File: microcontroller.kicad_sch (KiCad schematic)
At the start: 0 parts

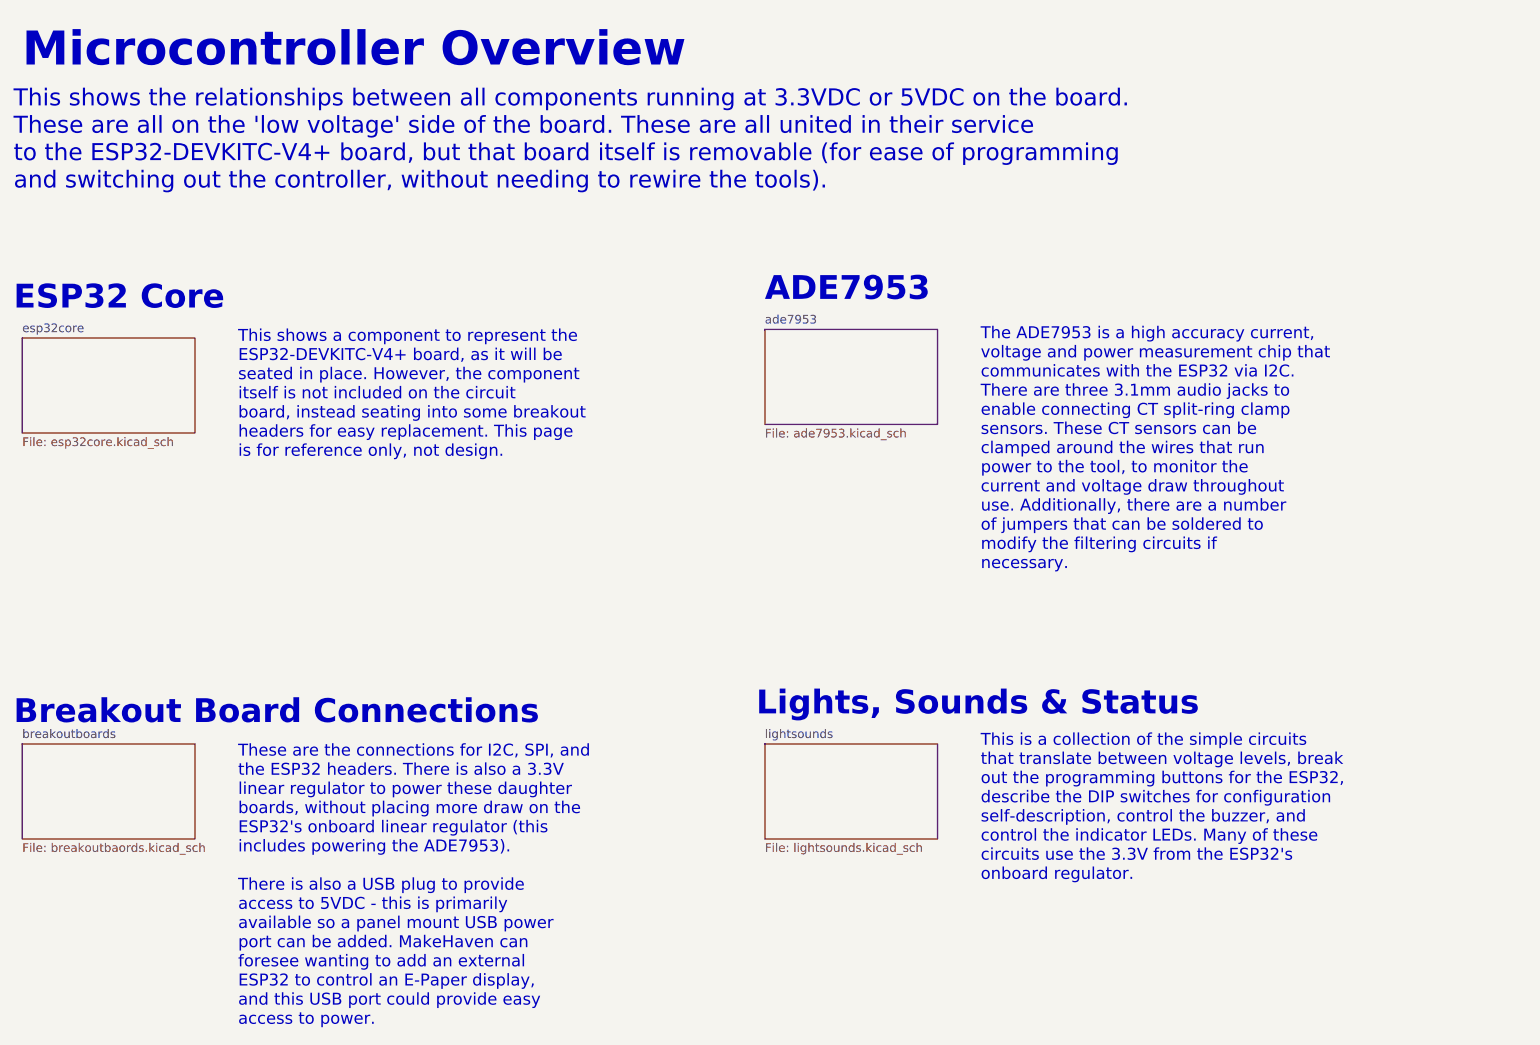
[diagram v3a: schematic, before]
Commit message: moved LED GPIO to fit free pins for ethernet wing
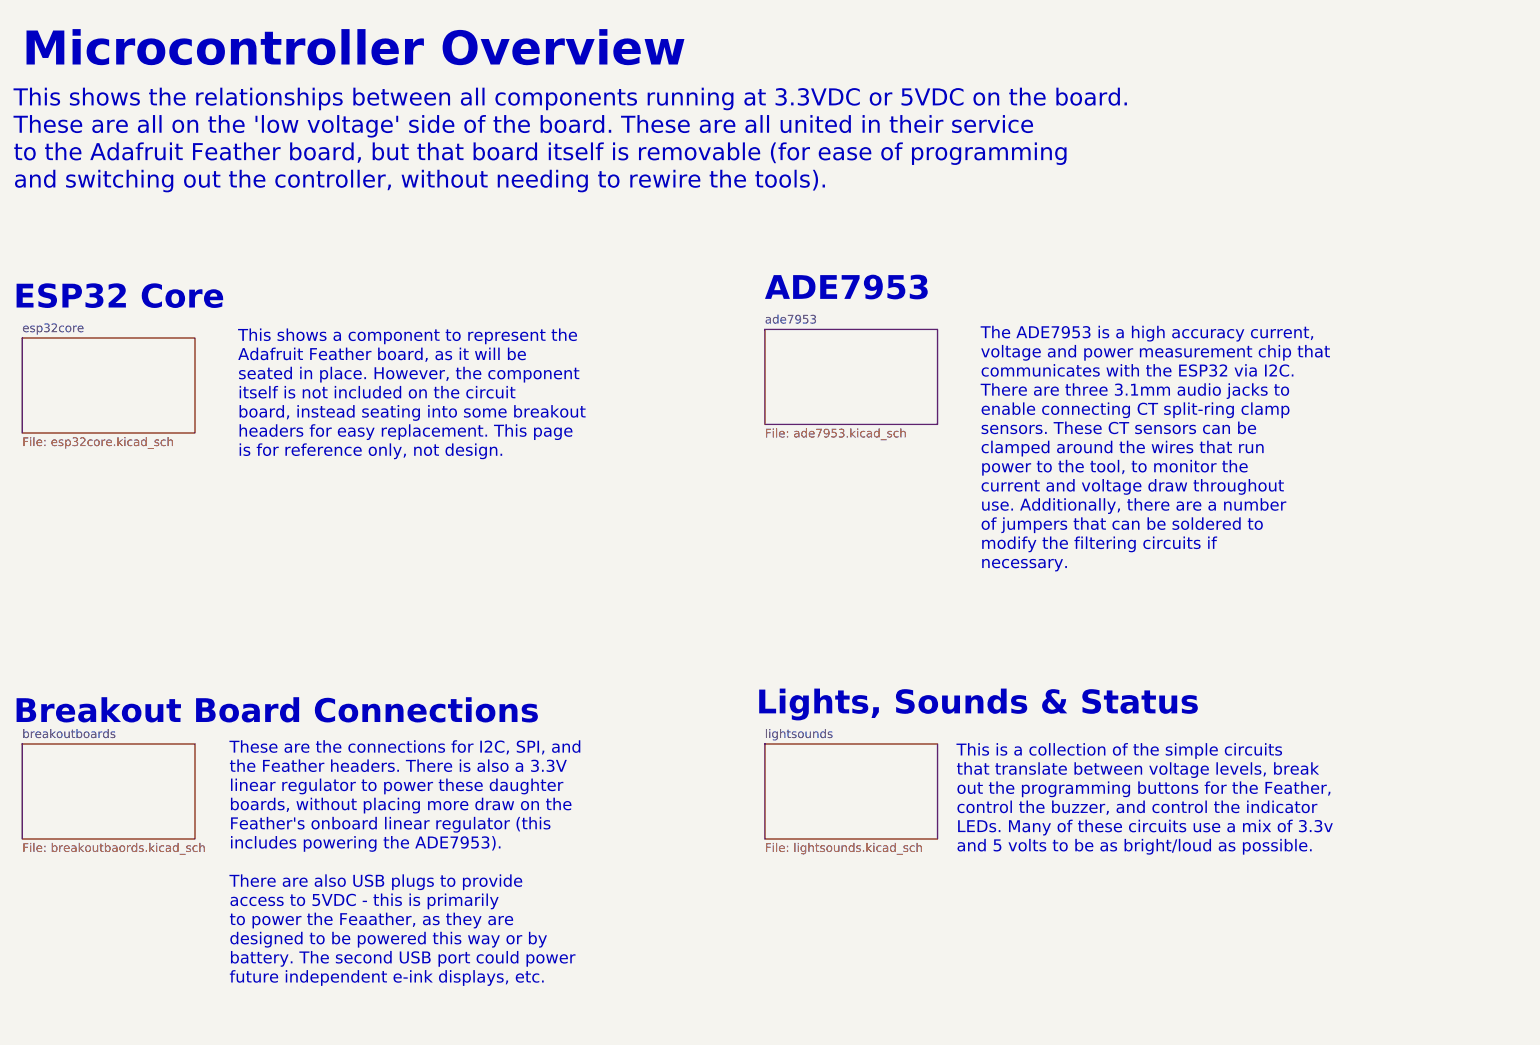
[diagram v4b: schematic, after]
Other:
- note added: "These are the connections for I2C, SPI, and the Feather headers. There is also a 3.3V linear regulator to power these daughter boards, without placing more draw on the Feather's onboard linear regulator (this includes powering the ADE7953). There are also USB plugs to provide access to 5VDC - this is primarily to power the Feaather, as they are designed to be powered this way or by battery. The s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"
- note added: "This is a collection of the simple circuits that translate between voltage levels, break out the programming buttons for the Feather, control the buzzer, and control the indicator LEDs. Many of these circuits use a mix of 3.3v and 5 volts to be as bright/loud as possible."
- note added: "This shows a component to represent the Adafruit Feather board, as it will be seated in place. However, the component itself is not included on the circuit board, instead seating into some breakout headers for easy replacement. This page is for reference only, not design."
- note added: "This shows the relationships between all components running at 3.3VDC or 5VDC on the board. These are all on the 'low voltage' side of the board. These are all united in their service to the Adafruit Feather board, but that board itself is removable (for ease of programming and switching out the controller, without needing to rewire the tools)."
- note removed: "These are the connections for I2C, SPI, and the ESP32 headers. There is also a 3.3V linear regulator to power these daughter boards, without placing more draw on the ESP32's onboard linear regulator (this includes powering the ADE7953). There is also a USB plug to provide access to 5VDC - this is primarily available so a panel mount USB power port can be added. MakeHaven can foresee wanting to ad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"
- note removed: "This is a collection of the simple circuits that translate between voltage levels, break out the programming buttons for the ESP32, describe the DIP switches for configuration self-description, control the buzzer, and control the indicator LEDs. Many of these circuits use the 3.3V from the ESP32's onboard regulator."
- note removed: "This shows a component to represent the ESP32-DEVKITC-V4+ board, as it will be seated in place. However, the component itself is not included on the circuit board, instead seating into some breakout headers for easy replacement. This page is for reference only, not design."
- note removed: "This shows the relationships between all components running at 3.3VDC or 5VDC on the board. These are all on the 'low voltage' side of the board. These are all united in their service to the ESP32-DEVKITC-V4+ board, but that board itself is removable (for ease of programming and switching out the controller, without needing to rewire the tools)."
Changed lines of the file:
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@@
 		(company "Corey Rice & MakeHaven")
 	)
-	(text "This shows the relationships between all components running at 3.3VDC or 5VDC on the board. \nThese are all on the 'low voltage' side of the board. These are all united in their service \nto the ESP32-DEVKITC-V4+ board, but that board itself is removable (for ease of programming \nand switching out the controller, without needing to rewire the tools). "
+	(text "This shows the relationships between all components running at 3.3VDC or 5VDC on the board. \nThese are all on the 'low voltage' side of the board. These are all united in their service \nto the Adafruit Feather board, but that board itself is removable (for ease of programming \nand switching out the controller, without needing to rewire the tools). "
 		(exclude_from_sim no)
 		(at 33.02 49.53 0)
@@
 		)
 	)
-	(text "This is a collection of the simple circuits \nthat translate between voltage levels, break \nout the programming buttons for the ESP32, \ndescribe the DIP switches for configuration \nself-description, control the buzzer, and \ncontrol the indicator LEDs. Many of these \ncircuits use the 3.3V from the ESP32's \nonboard regulator.\n"
+	(text "This is a collection of the simple circuits \nthat translate between voltage levels, break \nout the programming buttons for the Feather, \ncontrol the buzzer, and control the indicator \nLEDs. Many of these circuits use a mix of 3.3v\nand 5 volts to be as bright/loud as possible.\n"
 		(exclude_from_sim no)
-		(at 175.26 151.13 0)
+		(at 171.704 147.066 0)
 		(effects
 			(font
@@
 		)
 	)
-	(text "This shows a component to represent the \nESP32-DEVKITC-V4+ board, as it will be \nseated in place. However, the component \nitself is not included on the circuit \nboard, instead seating into some breakout \nheaders for easy replacement. This page \nis for reference only, not design."
+	(text "This shows a component to represent the \nAdafruit Feather board, as it will be \nseated in place. However, the component \nitself is not included on the circuit \nboard, instead seating into some breakout \nheaders for easy replacement. This page \nis for reference only, not design."
 		(exclude_from_sim no)
 		(at 66.04 88.9 0)
@@
 		)
 	)
-	(text "These are the connections for I2C, SPI, and \nthe ESP32 headers. There is also a 3.3V \nlinear regulator to power these daughter \nboards, without placing more draw on the \nESP32's onboard linear regulator (this \nincludes powering the ADE7953).\n\nThere is also a USB plug to provide \naccess to 5VDC - this is primarily \navailable so a panel mount USB power \nport can be added. MakeHaven can \nforesee wanting to add an external \nESP32 to control an E-Paper display, \nand this USB port could provide easy \naccess to power.\n\n"
+	(text "These are the connections for I2C, SPI, and \nthe Feather headers. There is also a 3.3V \nlinear regulator to power these daughter \nboards, without placing more draw on the \nFeather's onboard linear regulator (this \nincludes powering the ADE7953).\n\nThere are also USB plugs to provide \naccess to 5VDC - this is primarily \nto power the Feaather, as they are \ndesigned to be powered this way or by\nbattery. The second USB port could power \nfuture independent e-ink displays, etc.\n"
 		(exclude_from_sim no)
-		(at 66.04 175.26 0)
+		(at 64.77 166.37 0)
 		(effects
 			(font
